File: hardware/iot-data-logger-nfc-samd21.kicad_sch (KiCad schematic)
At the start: 50 parts, among them IC1 ST25DV04KC, IC2 BU27030NUC-E2, J1 ARM-JTAG-SWD-10, J2 USB_C_Receptacle_USB2.0, Q1 IRLML6401, U1 LD1117S33TR, U2 ATSAMD21E17D-AUT, U3 AT25DF041B-XMHN-B, U4 ATECC608A, U5 TPD2E009DBZR, U6 SHT30-DIS, U7 ICM-42670-P, Y1 32.768K-38-SR, Y2 KX-3HT 8.0 MHz

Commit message: add enclosure, bom docs
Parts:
- added TP1, TP2, TP3, TP4, TP5, TP6, TP7, TP8, TP9: TestPoint_Probe, TestPoint:TestPoint_THTPad_D1.0mm_Drill0.5mm, symbol Connector:TestPoint_Probe
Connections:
- net IMU_INT1: now also TP8.1
- net IMU_INT2: now also TP9.1
- net MISO: now also TP6.1
- net MOSI: now also TP3.1
- net NFC_INT: now also TP5.1
- net SCK: now also TP4.1
- net SCL: now also TP2.1
- net SDA: now also TP1.1
- net TEMP_INT: now also TP7.1
- net RESET renamed ~RESET
- net TEMP_RESET renamed ~TEMP_RESET
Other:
- note added: "С=28.5pF equivalent L=4.9uH"

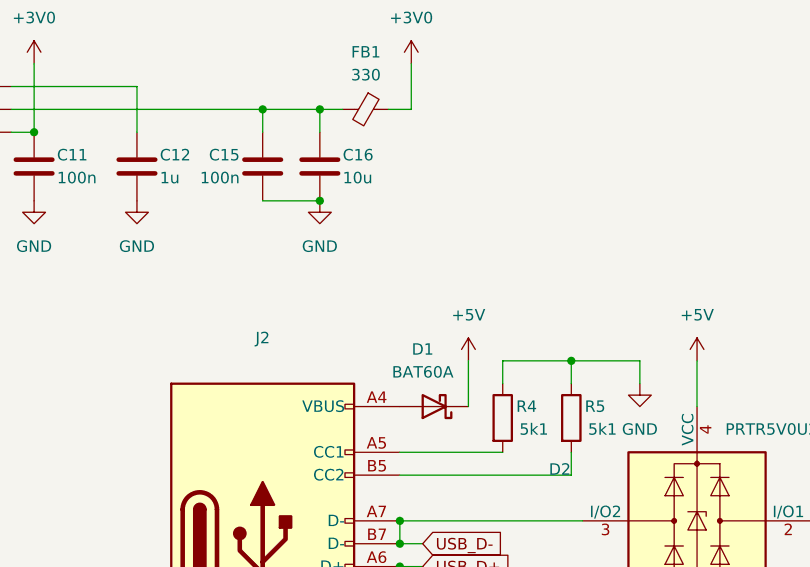
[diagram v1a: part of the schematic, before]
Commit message: configure SERCOM0, SERCOM1, RTC  peripherial libraries, draft FreeRTOS config
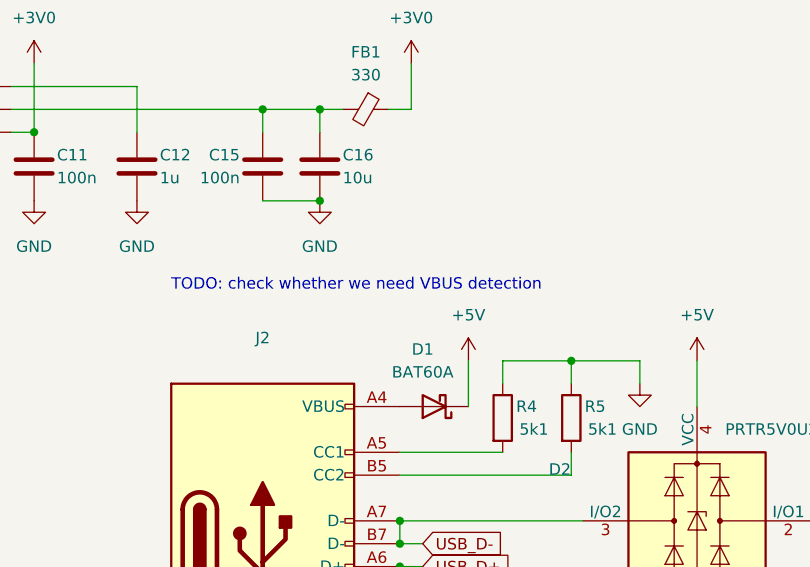
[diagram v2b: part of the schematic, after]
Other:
- note added: "TODO: check whether we need VBUS detection"
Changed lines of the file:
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@@
     (stroke (width 0) (type default) (color 0 0 0 0))
+  )
+  (text "TODO: check whether we need VBUS detection" (at 205.74 181.61 0)
+    (effects (font (size 1.27 1.27)) (justify left bottom))
   )
   (text "HARDWARE CRYPTO\n" (at 213.36 19.05 0)

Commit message: upgrade PCB with CS pin, NFC pull-up
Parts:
- removed C2, C4: 16p, Capacitor_SMD:C_0805_2012Metric_Pad1.18x1.45mm_HandSolder, symbol Device:C
- removed C21, C22: 100n, Capacitor_SMD:C_0805_2012Metric_Pad1.18x1.45mm_HandSolder, symbol Device:C
- removed U1: LD1117S33TR, Package_TO_SOT_SMD:SOT-223-3_TabPin2, symbol Regulator_Linear:LD1117S33TR_SOT223
- removed U7: ICM-42670-P, IC_ICM-42670-P, symbol ICM-42670-P:ICM-42670-P
- removed Y1: 32.768K-38-SR, Crystal:Crystal_C38-LF_D3.0mm_L8.0mm_Horizontal_1EP_style1, symbol Device:Crystal_GND3
- removed Y2: KX-3HT 8.0 MHz, Crystal:Crystal_HC49-U_Vertical, symbol Device:Crystal
- added C18: 10u, Capacitor_SMD:C_0805_2012Metric_Pad1.18x1.45mm_HandSolder, symbol Device:C
- added C20: 100n, Capacitor_SMD:C_0805_2012Metric_Pad1.18x1.45mm_HandSolder, symbol Device:C
- added D2: LED, LED_SMD:LED_0805_2012Metric_Pad1.15x1.40mm_HandSolder, symbol Device:LED
- added R1, R11, R2: 10k, Resistor_SMD:R_0805_2012Metric_Pad1.20x1.40mm_HandSolder, symbol Device:R
- added R8: 1k, Resistor_SMD:R_0805_2012Metric_Pad1.20x1.40mm_HandSolder, symbol Device:R
- added TP10: TestPoint_Probe, TestPoint:TestPoint_THTPad_D1.0mm_Drill0.5mm, symbol Connector:TestPoint_Probe
- added U1: L78L33_SOT89, Package_TO_SOT_SMD:SOT-89-3, symbol Regulator_Linear:L78L33_SOT89
- added U7: MMA8452Q, footprints:QFN-16_0.5MM-EXTRA, symbol MMA8452Q:MMA8452Q
- added Y1: KX-327NHT, Crystal:Crystal_SMD_EuroQuartz_EQ161-2Pin_3.2x1.5mm_HandSoldering, symbol Device:Crystal
- D1: footprint Diode_SMD:D_SOD-323 -> Diode_SMD:D_SOD-323_HandSoldering
- renumbered C13 to C10, C12 to C11, C14 to C12, C15 to C13, C16 to C14, C17 to C15, C18 to C16, C3 to C2, C20 to C21, C5 to C3, C6 to C4, C7 to C5, C9 to C6, C8 to C7, C10 to C8, C11 to C9, D2 to D3, R7 to R10, R1 to R3, R2 to R4, R3 to R5, R4 to R6, R5 to R7, R6 to R9, TP6 to TP5, TP5 to TP6
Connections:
- net +3V0: now also C18.1, R11.1, R8.1, U1.1 (OUT), U7.1 (VDDIO), U7.14 (VDD)
- net +5V: now also Q1.1 (G), R1.1, U1.3 (IN)
- net FLASH_CS: now also TP10.1
- net GND: now also C18.2, C20.2, R2.2, U1.2 (GND), U7.10 (GND@1), U7.12 (GND@2), U7.5 (GND@0), U7.7 (SA0); no longer Q1.1 (G)
- net IMU_INT1: now also U7.9 (INT2)
- net IMU_INT2: now also U7.11 (INT1)
- net NFC_INT: now also R11.2
- net SCL: now also U7.4 (SCL)
- net SDA: now also U7.6 (SDA)
- net XIN32: now also Y1.1
- net XOUT32: now also Y1.2
- net _TEMP_RESET: now reaches U2.21 (PA22/VDDIO/EXTINT[6]/X[10]/SERCOM3/PAD[0]/SERCOM5/PAD[0]/TC4/WO[0]/TCC0/WO[4]/GCLK_IO[6])
- net _TEMP_RESET: now also U6.6 (~{RESET})
- net LED: now reaches U2.22 (PA23/VDDIO/EXTINT[7]/X[11]/SERCOM3/PAD[1]/SERCOM5/PAD[1]/TC4/WO[1]/TCC0/WO[5]/USB/SOF1KHZ/GCLK_IO[7])
- net LED: now also D2.1 (K)
- net USB_VBUS_SENSE: now reaches U2.25 (PA27/VDDIO/EXTINT[15]/GCLK_IO[0])
- net USB_VBUS_SENSE: now also R1.2, R2.1
- net XIN: no longer names the net of U2.15 (PA14/VDDIO/EXTINT[14]/SERCOM2/PAD[2]/SERCOM4/PAD[2]/TC3/WO[0]/TCC0/WO[4]/GCLK_IO[0])
- net XOUT: no longer names the net of U2.16 (PA15/VDDIO/EXTINT[15]/SERCOM2/PAD[3]/SERCOM4/PAD[3]/TC3/WO[1]/TCC0/WO[5]/GCLK_IO[1])
- net ~TEMP_RESET: no longer names the net of U2.5 (PA04/VDDANA/EXTINT[4]/ADC/VREFB/AIN[4]/AIN[0]/Y[2]/SERCOM0/PAD[0]/TCC0/WO[0])
- net ~TEMP_RESET: no longer U6.6 (~{RESET})
- new net: C20.1, U7.2 (BYP)
- new net: D2.2 (A), R8.2
- no-connect marks 22 -> 17
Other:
- note removed: "TODO: check whether we need VBUS detection"
- moved on the sheet: BT1, BT2, C3, C4, C5, C7, F1, Q1, TP1, TP2, TP3, TP4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

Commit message: shematics, PCB, BOM: update, prepare for SMT order, change light sensor to OPT3001
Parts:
- removed BT1, BT2: LR03 AAA 1Ah, footprints:BAT-AAA-LR03, symbol Device:Battery_Cell
- removed C7: 10u, Capacitor_SMD:C_0805_2012Metric_Pad1.18x1.45mm_HandSolder, symbol Device:C
- removed IC2: BU27030NUC-E2, SON50P210X200X60-9N, symbol BU27030NUC-E2:BU27030NUC-E2
- removed J1: ARM-JTAG-SWD-10, Connector_PinHeader_2.54mm:PinHeader_2x05_P2.54mm_Vertical, symbol Connector:Conn_ARM_JTAG_SWD_10
- removed R11: 10k, Resistor_SMD:R_0805_2012Metric_Pad1.20x1.40mm_HandSolder, symbol Device:R
- removed TP10, TP3, TP4, TP5, TP7: TestPoint_Probe, TestPoint:TestPoint_THTPad_D1.0mm_Drill0.5mm, symbol Connector:TestPoint_Probe
- removed U5: TPD2E009DBZR, Package_TO_SOT_SMD:SOT-23, symbol Power_Protection:TPD2EUSB30A
- added BT1: 2xAAA, Battery:BatteryHolder_Keystone_2468_2xAAA, symbol Device:Battery
- added H1, H2, H3, H4: MountingHole_Pad, MountingHole:MountingHole_3.2mm_M3_Pad_Via, symbol Mechanical:MountingHole_Pad
- added J1: Pickit 5 Conn, Connector_PinSocket_2.54mm:PinSocket_1x08_P2.54mm_Vertical, symbol Connector:Conn_01x08_Socket
- added NT1, NT2, NT3, NT4, NT5: NetTie_2, NetTie:NetTie-2_SMD_Pad0.5mm, symbol Device:NetTie_2
- added TP11: TestPoint_Probe, TestPoint:TestPoint_THTPad_D1.5mm_Drill0.7mm, symbol Connector:TestPoint_Probe
- added U8: OPT3001DNPR, Personal:SON65P200X200X65-7N, symbol OPT3001DNPR:OPT3001DNPR
- AE1: now left out of the parts list
- C1, C2: value 12p -> 22p; LCSC Part (none) -> C1804; Part (none) -> CL21C220JBANNNC; URL (none) -> https://www.lcsc.com/product-detail/Multilayer-Ceramic-Capa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
- C10, C13, C15, C16, C19, C20, C21, C4, C6, C8, C9: LCSC Part (none) -> C1711; Part (none) -> CL21B104KBCNNNC; URL (none) -> https://www.lcsc.com/product-detail/Multilayer-Ceramic-Capa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
- C11: value 1u -> 10u; LCSC Part (none) -> C1713; Part (none) -> CL21A106KOQNNNE; URL (none) -> https://www.lcsc.com/product-detail/Multilayer-Ceramic-Capa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
- C12: LCSC Part (none) -> C50131; Part (none) -> CL21B472KBANNNC; URL (none) -> https://www.lcsc.com/product-detail/Multilayer-Ceramic-Capa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
- C14, C5: LCSC Part (none) -> C1713; Part (none) -> CL21A106KOQNNNE; URL (none) -> https://www.lcsc.com/product-detail/Multilayer-Ceramic-Capa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
- C18: value 10u -> 100n; LCSC Part (none) -> C1711; Part (none) -> CL21B104KBCNNNC; URL (none) -> https://www.lcsc.com/product-detail/Multilayer-Ceramic-Capa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
- C3: LCSC Part (none) -> C12891; Part (none) -> CL31A226KAHNNNE; URL (none) -> https://www.lcsc.com/product-detail/Multilayer-Ceramic-Capa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
- D1: LCSC Part (none) -> C5355496; Part (none) -> BAT60A; URL (none) -> https://www.lcsc.com/product-detail/Schottky-Barrier-Diodes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
- D2: LCSC Part (none) -> C84260; Part (none) -> NCD0805G1; URL (none) -> https://www.lcsc.com/product-detail/Light-Emitting-Diodes-L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
- D3: LCSC Part (none) -> C2827688; Part (none) -> PRTR5V0U2X; URL (none) -> https://www.lcsc.com/product-detail/ESD-Protection-Devices_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
- F1: footprint Capacitor_SMD:C_1812_4532Metric_Pad1.57x3.40mm_HandSolder -> Fuse:Fuse_1812_4532Metric_Pad1.30x3.40mm_HandSolder; LCSC Part (none) -> C12430; Part (none) -> MF-MSMF010-2; URL (none) -> https://www.lcsc.com/product-detail/Resettable-Fuses_BOURNS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
- FB1: LCSC Part (none) -> C47130; Part (none) -> BLM21PG331SN1D; URL (none) -> https://www.lcsc.com/product-detail/Ferrite-Beads_Murata-El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
- J2: value USB_C_Receptacle_USB2.0 -> USB Type-C; LCSC Part (none) -> C709357; Part (none) -> KH-TYPE-C-16P; URL (none) -> https://www.lcsc.com/product-detail/USB-Connectors_Shenzhen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
- Q1: LCSC Part (none) -> C3034; Part (none) -> IRLML6401TRPBF; URL (none) -> https://www.lcsc.com/product-detail/MOSFETs_Infineon-Techno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
- R1, R2, R4: LCSC Part (none) -> C84376; Part (none) -> RC0805FR-0710KL; URL (none) -> https://www.lcsc.com/product-detail/Chip-Resistor-Surface-M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
- R10, R9: LCSC Part (none) -> C60816; Part (none) -> RC0805FR-074K7L; URL (none) -> https://www.lcsc.com/product-detail/Chip-Resistor-Surface-M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
- R3, R8: LCSC Part (none) -> C95781; Part (none) -> RC0805FR-071KL; URL (none) -> https://www.lcsc.com/product-detail/Chip-Resistor-Surface-M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
- R5: LCSC Part (none) -> C107700; Part (none) -> RC0805FR-071ML; URL (none) -> https://www.lcsc.com/product-detail/Chip-Resistor-Surface-M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
- R6, R7: LCSC Part (none) -> C84375; Part (none) -> RC0805FR-075K1L; URL (none) -> https://www.lcsc.com/product-detail/Chip-Resistor-Surface-M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
- TP1, TP2, TP6, TP8, TP9: footprint TestPoint:TestPoint_THTPad_D1.0mm_Drill0.5mm -> TestPoint:TestPoint_THTPad_D1.5mm_Drill0.7mm; now left out of the parts list
- U1: value L78L33_SOT89 -> L78L33ABUTR; footprint Package_TO_SOT_SMD:SOT-89-3 -> Package_TO_SOT_SMD:SOT-89-3_Handsoldering; LCSC Part (none) -> C81362; Part (none) -> L78L33ABUTR; URL (none) -> https://www.lcsc.com/product-detail/Linear-Voltage-Regulato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
- U2: value ATSAMD21E17D-AUT -> ATSAMD21E18A-AU; footprint QFP80P900X900X120-32N -> Package_QFP:TQFP-32_7x7mm_P0.8mm; LCSC Part (none) -> C618771; LCSC Part ALT (none) -> C618770; MANUFACTURER Microchip -> (none); Manufacturer (none) -> Microchip; Part (none) -> ATSAMD21E18A-AU; STANDARD IPC-7351B -> (none); URL (none) -> https://www.lcsc.com/product-detail/Microcontroller-Units-M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; URL ALT (none) -> https://www.lcsc.com/product-detail/Microcontroller-Units-M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
- U3: value AT25DF041B-XMHN-B -> AT25DF321; footprint Package_SO:TSSOP-8_4.4x3mm_P0.65mm -> Package_SO:SOP-8_5.28x5.23mm_P1.27mm; LCSC Part (none) -> C6490; MANUFACTURER Dialog Semiconductor -> (none); MAXIMUM_PACKAGE_HEIGHT 1.2 mm -> (none); PARTREV 5/2017 -> (none); Part (none) -> AT25DF321A-SH-T; STANDARD Manufacturer Recommendations -> (none); URL (none) -> https://www.lcsc.com/product-detail/NOR-FLASH_Dialog-Semico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
- U4: value ATECC608A -> ATECC608A-MAHDA-S; footprint Package_SO:SOIC-8_3.9x4.9mm_P1.27mm -> Package_DFN_QFN:DFN-8-1EP_3x2mm_P0.5mm_EP1.3x1.5mm; LCSC Part (none) -> C616908; Part (none) -> ATECC608A-MAHDA-S; URL (none) -> https://www.lcsc.com/product-detail/Security-Verification-E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
- U6: LCSC Part (none) -> C2687423; Part (none) -> SHT30-DIS-B10KS; URL (none) -> https://www.lcsc.com/product-detail/Temperature-and-Humidit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
- U7: value MMA8452Q -> MMA8452QR1; footprint footprints:QFN-16_0.5MM-EXTRA -> Personal:XDCR_MMA8452QR1; LCSC Part (none) -> C11360; Part (none) -> MMA8452QR1; URL (none) -> https://www.lcsc.com/product-detail/Attitude-Sensor-Gyrosco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
- U9: renamed from IC1; value ST25DV04KC -> ST25DV04K; Arrow Part Number ST25DV64K-IER8T3 -> (none); Arrow Price/Stock https://www.arrow.com/en/products/st25dv64k-ier8t3/stmicroe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 -> (none); Height 1.2 -> (none); LCSC Part (none) -> C2654816; Manufacturer (none) -> STMicroelectronics; Manufacturer_Name STMicroelectronics -> (none); Manufacturer_Part_Number ST25DV64K-IER8T3 -> (none); Mouser Part Number 511-ST25DV64K-IER8T3 -> (none); Mouser Price/Stock https://www.mouser.co.uk/ProductDetail/STMicroelectronics/S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 -> (none); Part (none) -> ST25DV04K-IER6T3; URL (none) -> https://www.lcsc.com/product-detail/RF-Chips_STMicroelectro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
- Y1: value KX-327NHT -> SC-32S32.768; LCSC Part (none) -> C97606; Part (none) -> SC-32S32.768kHz20PPM12.5pF; URL (none) -> https://www.lcsc.com/product-detail/Crystals_Seiko-SC-32S32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
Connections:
- net +3V0: now also J1.2 (Pin_2), NT1.1, NT2.1, NT3.2, NT4.1, NT5.2; no longer U4.8 (VCC), U6.5 (VDD), U7.1 (VDDIO), U7.14 (VDD), U9.8 (VCC)
- net GND: now also BT1.2 (-), H1.1, H2.1, H3.1, H4.1, J1.3 (Pin_3), U8.2 (ADDR), U8.3 (GND), U8.7 (EXP)
- net IMU_INT1: now also U2.8 (PA07/VDDANA/EXTINT[7]/AIN[7]/AIN[3]/Y[5]/SERCOM0/PAD[3]/TCC1/WO[1]/I2S/SD[0]); no longer U2.7 (PA06/VDDANA/EXTINT[6]/AIN[6]/AIN[2]/Y[4]/SERCOM0/PAD[2]/TCC1/WO[0])
- net IMU_INT2: now also U2.7 (PA06/VDDANA/EXTINT[6]/AIN[6]/AIN[2]/Y[4]/SERCOM0/PAD[2]/TCC1/WO[0]); no longer U2.8 (PA07/VDDANA/EXTINT[7]/AIN[7]/AIN[3]/Y[5]/SERCOM0/PAD[3]/TCC1/WO[1]/I2S/SD[0])
- net SCL: now also U8.4 (SCL)
- net SDA: now also U8.6 (SDA)
- net SWDCLK: now also J1.5 (Pin_5)
- net SWDIO: now also J1.8 (Pin_8)
- net ~RESET: now also J1.1 (Pin_1)
- net at F1.2: now also BT1.1 (+)
- net LIGHT_INT: now reaches U2.13 (PA10/VDDIO/EXTINT[10]/AIN[18]/X[2]/SERCOM0/PAD[2]/SERCOM2/PAD[2]/TCC1/WO[0]/TCC0/WO[2]/I2S/SCK[0]/GCLK_IO[4])
- net LIGHT_INT: now also TP11.1, U8.5 (INT)
- net FLASH_CS renamed ~FLASH_CS
- net _TEMP_RESET renamed ~TEMP_RESET
- new net: NT1.2, U4.8 (VCC)
- new net: NT3.1, U9.8 (VCC)
- new net: NT5.1, U6.5 (VDD)
- new net: NT2.2, U7.1 (VDDIO), U7.14 (VDD)
- new net: NT4.2, U8.1 (VDD)
- no-connect marks 17 -> 14
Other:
- note added: "3-AXIS ACCELEROMETER"
- note added: "PICKIT"
- note added: "Should be 2V4+ flash, AT25DF is 2V6+"
- moved on the sheet: C1, C12, D1, D2, D3, F1, J2, R3, R5, R6, R9, TP1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

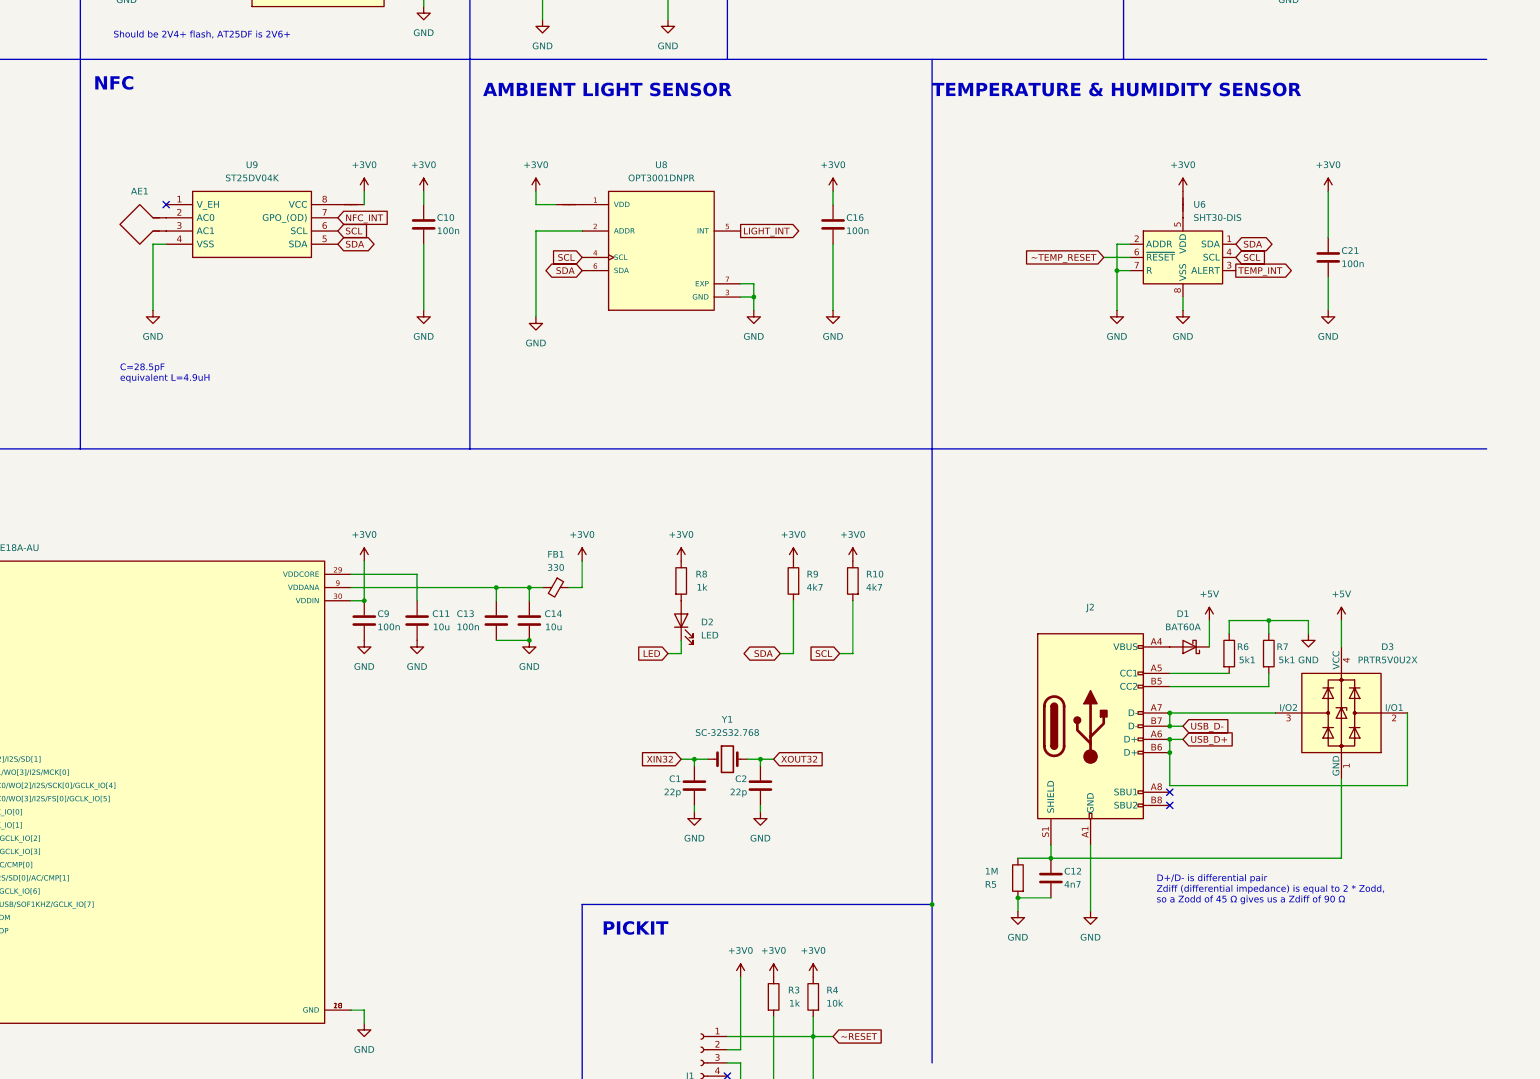
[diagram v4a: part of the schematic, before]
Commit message: update hardware, add enclosure drawings
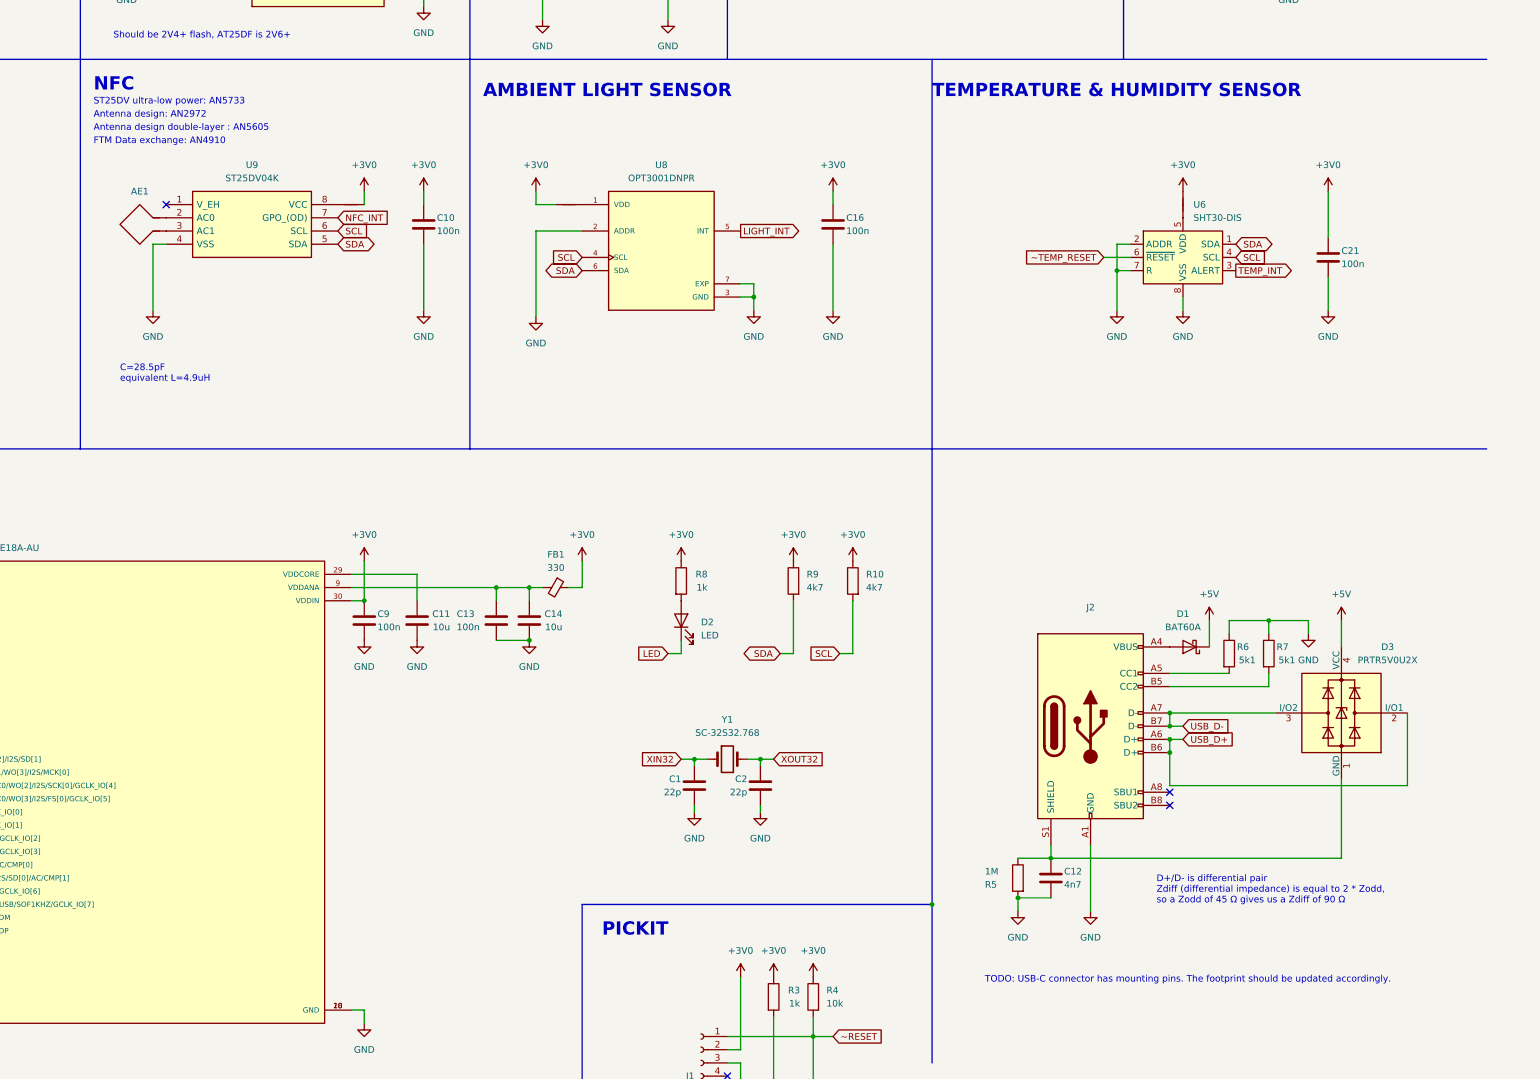
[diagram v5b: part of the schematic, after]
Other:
- note added: "Antenna design double-layer : AN5605"
- note added: "Antenna design: AN2972"
- note added: "FTM Data exchange: AN4910"
- note added: "ST25DV ultra-low power: AN5733"
- note added: "TODO: USB-C connector has mounting pins. The footprint should be updated accordingly."
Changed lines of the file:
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@@
     (stroke (width 0) (type default))
+  )
+  (text "Antenna design double-layer : AN5605" (at 138.43 73.66 0)
+    (effects (font (size 1.27 1.27)) (justify left bottom) (href "https://www.st.com/resource/en/application_note/an5605-design-of-a-1356-mhz-doublelayer-antenna-stmicroelectronics.pdf"))
   )
   (text "HARDWARE CRYPTO\n" (at 213.36 19.05 0)
     (effects (font (size 2.54 2.54) (thickness 0.508) bold) (justify left bottom))
+  )
+  (text "FTM Data exchange: AN4910" (at 138.43 76.2 0)
+    (effects (font (size 1.27 1.27)) (justify left bottom) (href "https://www.st.com/resource/en/application_note/an4910-data-exchange-between-wired-ic-and-wireless-rf-iso-15693-using-fast-transfer-mode-supported-by-st25dvi2c-series-stmicroelectronics.pdf"))
+  )
+  (text "TODO: USB-C connector has mounting pins. The footprint should be updated accordingly."
+    (at 309.88 237.49 0)
+    (effects (font (size 1.27 1.27)) (justify left bottom))
   )
   (text "NFC\n" (at 138.43 66.04 0)
@@
     (effects (font (size 1.27 1.27)) (justify left bottom))
   )
+  (text "Antenna design: AN2972" (at 138.43 71.12 0)
+    (effects (font (size 1.27 1.27)) (justify left bottom) (href "https://www.st.com/resource/en/application_note/an2972-how-to-design-an-antenna-for-dynamic-nfc-tags-stmicroelectronics.pdf"))
+  )
   (text "POWER" (at 15.24 19.05 0)
     (effects (font (size 2.54 2.54) (thickness 0.508) bold) (justify left bottom))
   )
+  (text "ST25DV ultra-low power: AN5733" (at 138.43 68.58 0)
+    (effects (font (size 1.27 1.27)) (justify left bottom) (href "https://www.st.com/resource/en/application_note/an5733-using-st25dvi2c-series-for-ultralow-power-applications-stmicroelectronics.pdf"))
+  )
   (text "Should be 2V4+ flash, AT25DF is 2V6+" (at 142.24 55.88 0)
